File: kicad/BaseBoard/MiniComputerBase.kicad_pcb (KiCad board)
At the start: 4 copper layers, 156.2 x 78.7 mm, 50 parts, among them J1 VIN, J2 PWRALT, J3 RESET, J4 Control and Data, J5 Address Bus, J6 Chip Selects, J7 PA/PB, J8 Power, J9 Power, SW1 POWER, SW2 RESET, U1 L78L33, U2 LM7805, U3 DS1813-5+, U4 W65C02SxP, U5 74LS00, U6 ATF22V10C, U7 62256, U8 28C256, U9 W65C22NxP, X1 XTAL, X2 XTAL_ALT

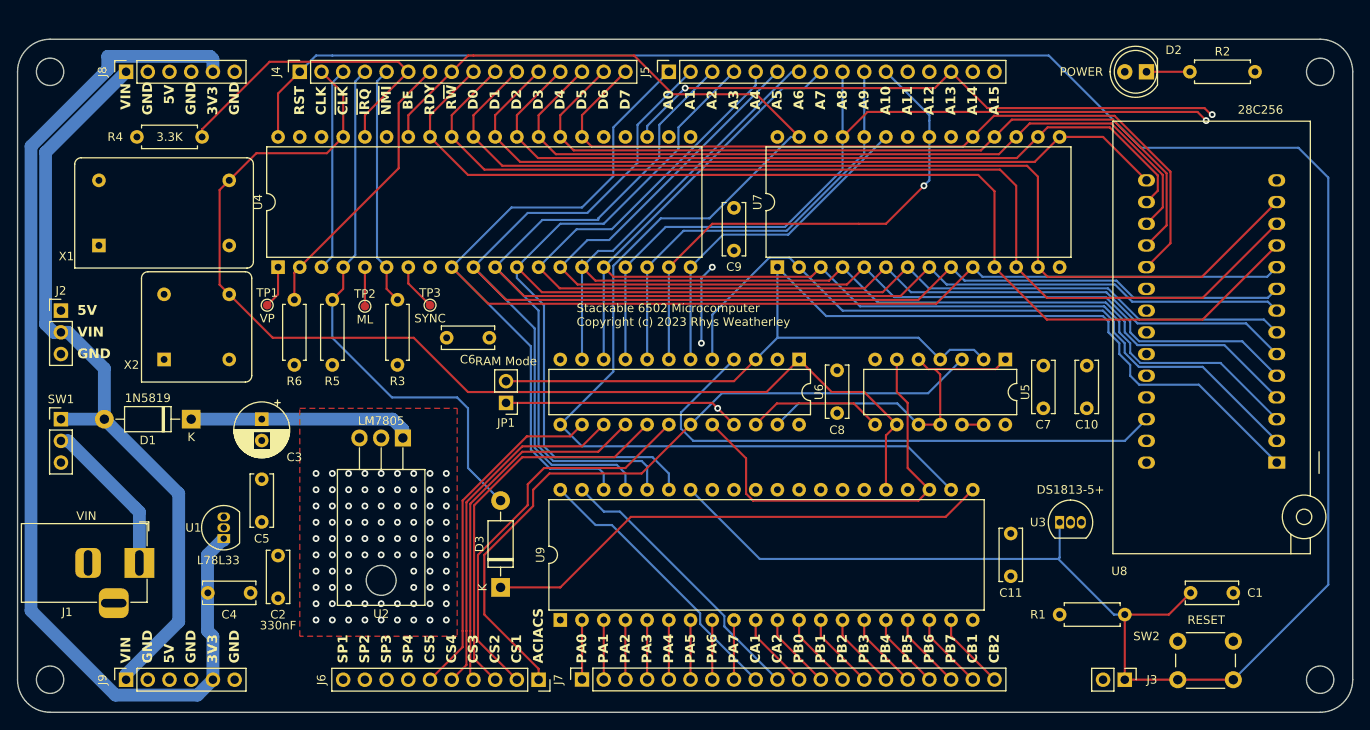
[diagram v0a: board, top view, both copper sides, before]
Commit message: I/O board schematic and layout
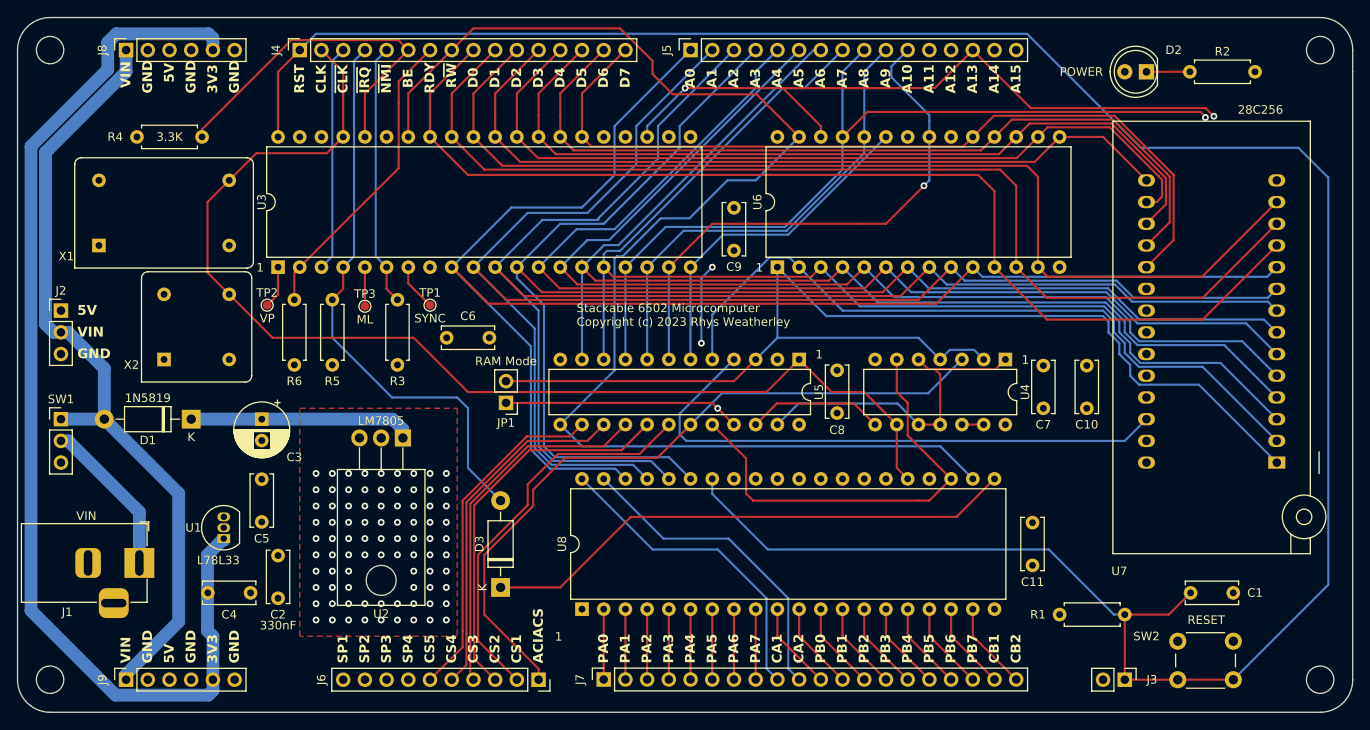
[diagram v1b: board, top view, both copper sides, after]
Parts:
- removed the U3 at (182.9, 83.2)
- moved J5 3.59 mm to (139.7, 27.9)
- moved C11 2.84 mm to (179.7, 88.2)
- moved U8 2.84 mm to (127.0, 93.3)
- moved H1 2.54 mm to (64.8, 27.9)
- moved H2 2.54 mm to (213.4, 27.9)
- moved J4 2.54 mm to (94.0, 27.9)
- moved J8 2.54 mm to (73.7, 27.9)
- moved J7 2.54 mm to (129.5, 101.6)
- renumbered TP3 to TP1, TP1 to TP2, TP2 to TP3, U4 to U3, U5 to U4, U6 to U5, U7 to U6, U8 to U7, U9 to U8
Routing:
- net a13: track 232.4 -> 224.6 mm
- net RW: track 153.1 -> 160.5 mm
- net a15: track 119.5 -> 124.6 mm
- net Net-(J7-Pin_9): track 32.8 -> 37.4 mm
- net a0: track 176.0 -> 180.5 mm
- net a3: track 170.9 -> 175.4 mm
- net a1: track 174.4 -> 178.9 mm
- net a7: track 134.1 -> 138.6 mm
- net Net-(J7-Pin_10): track 32.8 -> 37.2 mm
- net a14: track 210.4 -> 214.6 mm
- net a2: track 173.0 -> 177.0 mm
- net a8: track 132.2 -> 136.0 mm
- net a9: track 125.1 -> 128.9 mm
- net a4: track 128.4 -> 132.2 mm
- net a5: track 126.4 -> 130.0 mm
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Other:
- board size 156.2 x 78.7 mm -> 156.2 x 81.3 mm
- board text added: "1"
